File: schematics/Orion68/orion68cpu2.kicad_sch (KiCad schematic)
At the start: 46 parts, among them J1 clock, Q1 2N3904, Q2 2N3904, Q3 2N3904, SW2 reset, U0 74LS393, U1 MC68000P, U2 74LS541, U3 74LS541, U4 74LS541, U5 74LS245, U6 74LS245, U7 74LS541, U8 74LS148, Y1.2 16MHZ, Y2 16MHZ

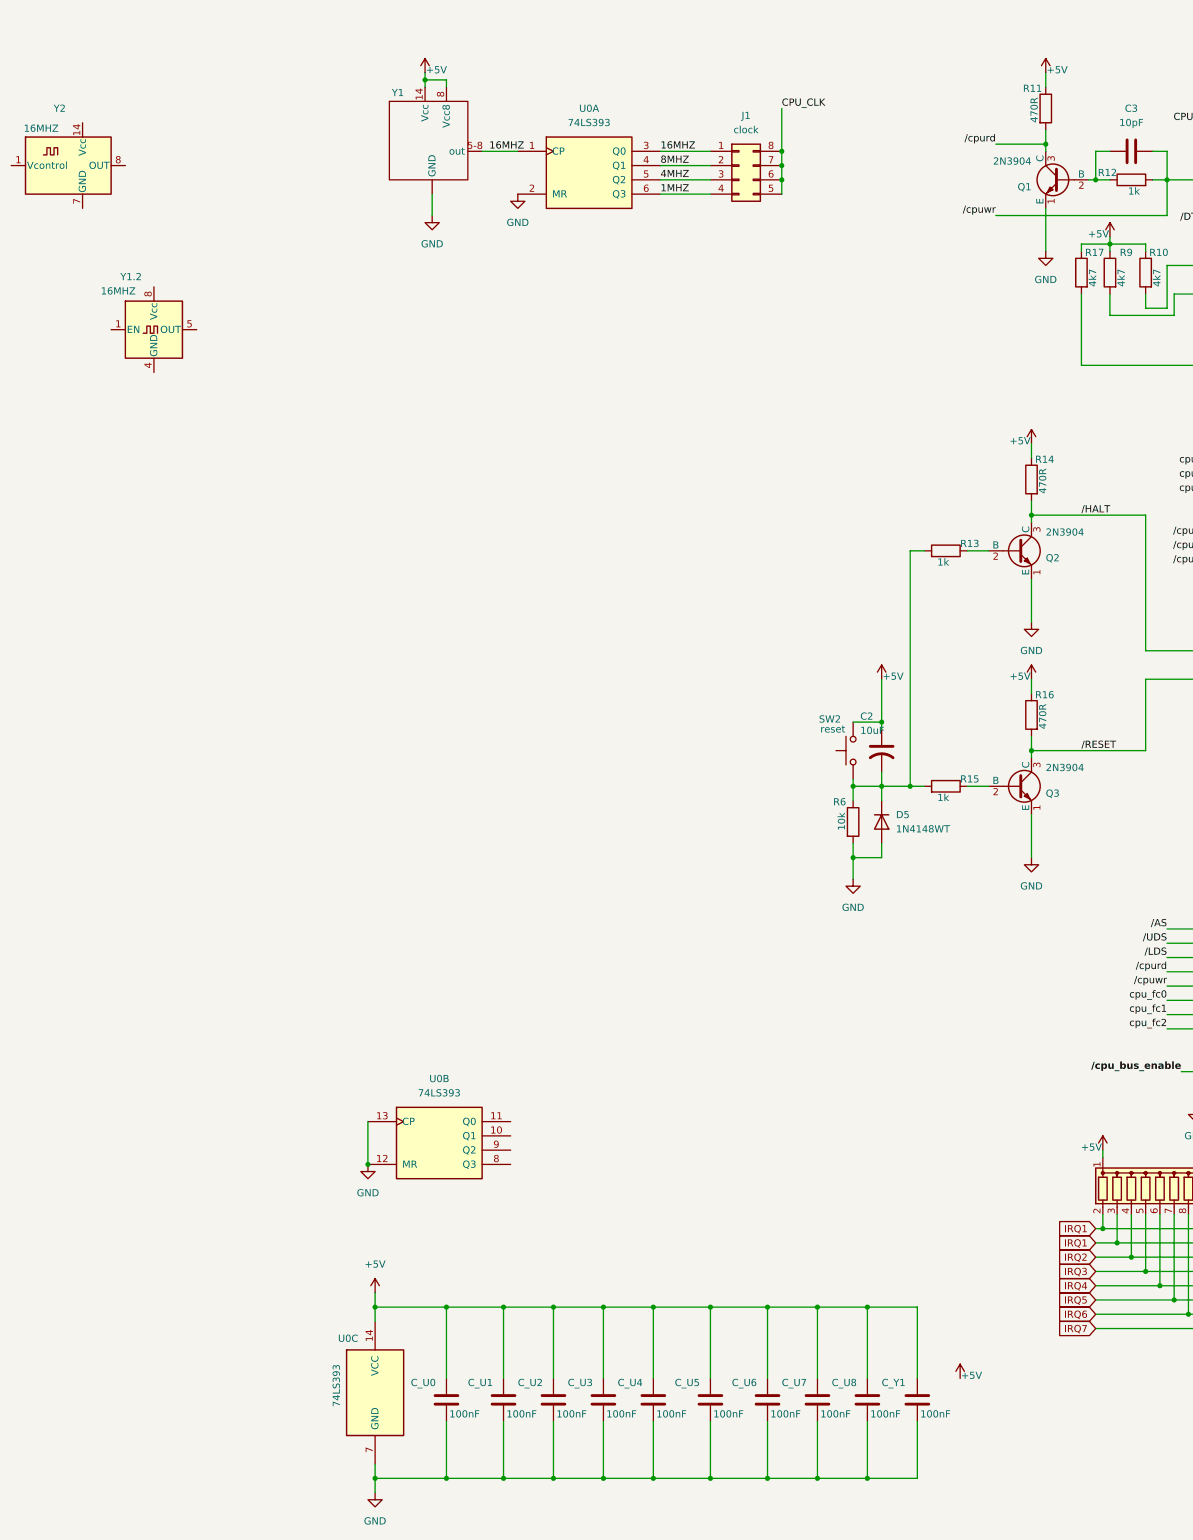
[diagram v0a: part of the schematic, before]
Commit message: Finished CPU board schematic
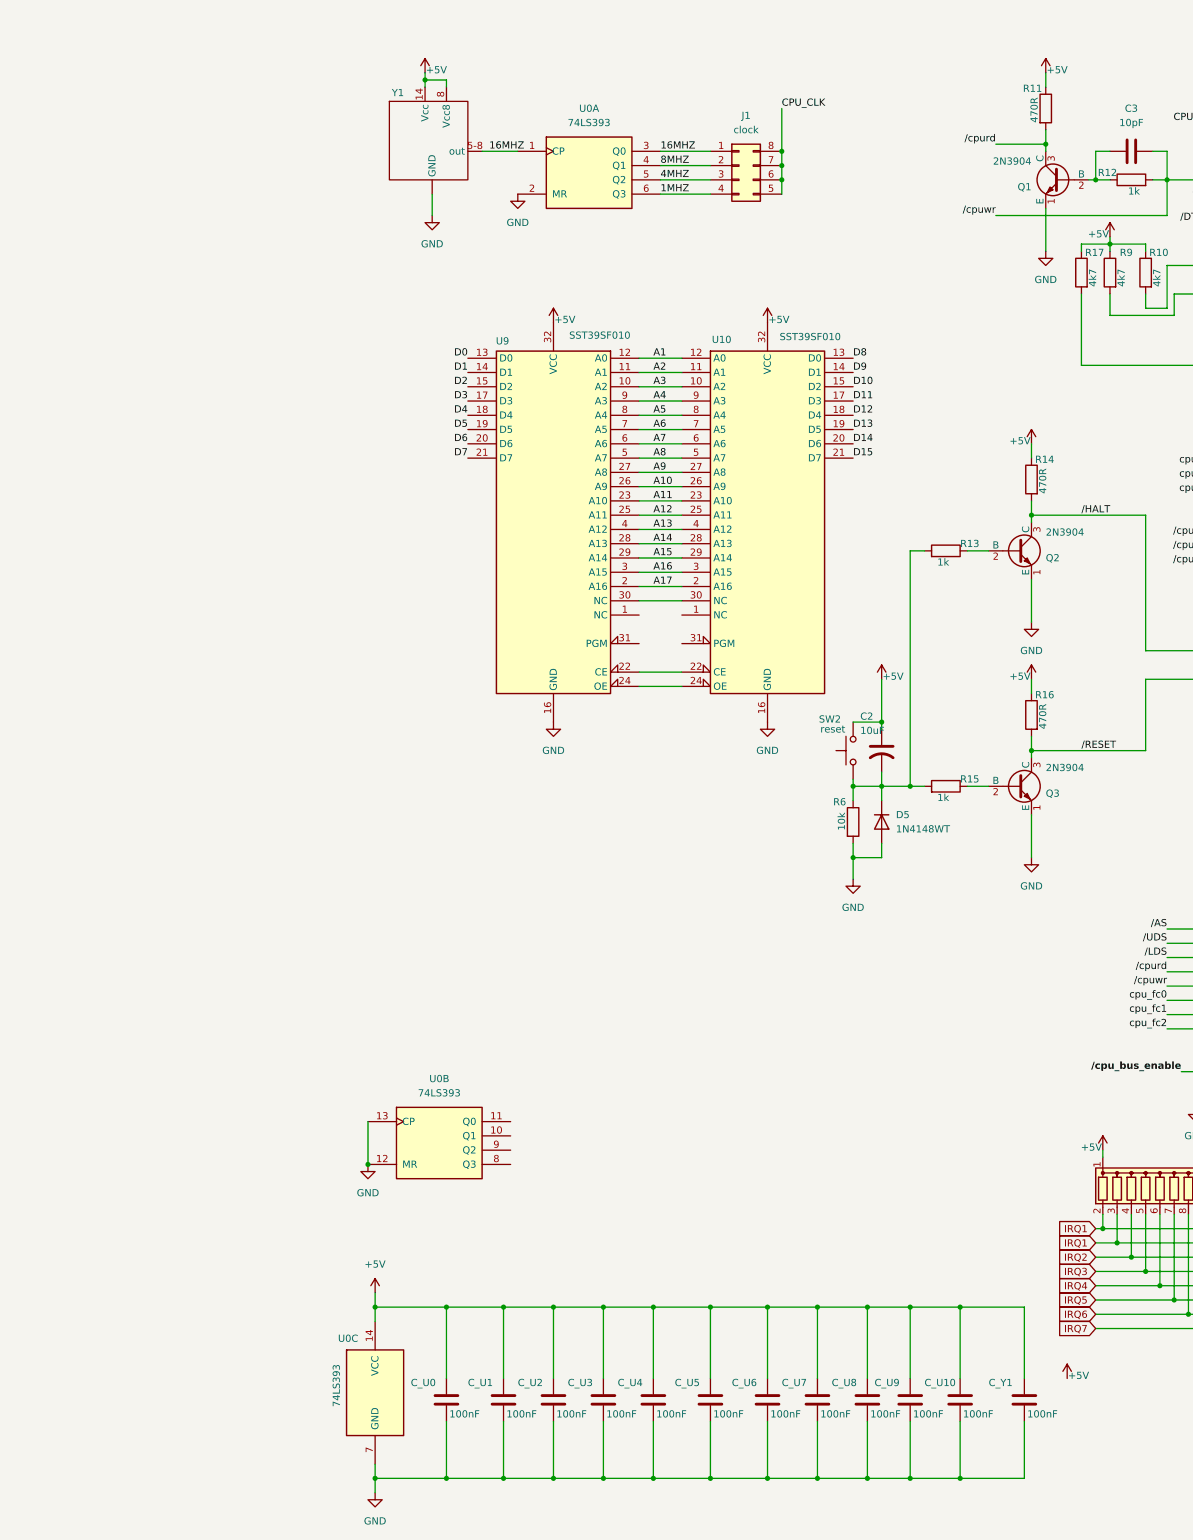
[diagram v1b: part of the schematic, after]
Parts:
- removed Y1.2: 16MHZ, Oscillator:Oscillator_DIP-8, symbol Oscillator:CXO_DIP8
- removed Y2: 16MHZ, Oscillator:Oscillator_DIP-14, symbol Oscillator:OCXO-14
- added C_U10, C_U9: 100nF, symbol Device:C
- added U10, U9: SST39SF010, symbol Memory_Flash:SST39SF010
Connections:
- net +5V: now also C_U10.1, C_U9.1, U10.32 (VCC), U9.32 (VCC)
- net A1: now also U10.12 (A0), U9.12 (A0)
- net A10: now also U10.26 (A9), U9.26 (A9)
- net A11: now also U10.23 (A10), U9.23 (A10)
- net A12: now also U10.25 (A11), U9.25 (A11)
- net A13: now also U10.4 (A12), U9.4 (A12)
- net A14: now also U10.28 (A13), U9.28 (A13)
- net A15: now also U10.29 (A14), U9.29 (A14)
- net A16: now also U10.3 (A15), U9.3 (A15)
- net A17: now also U10.2 (A16), U9.2 (A16)
- net A2: now also U10.11 (A1), U9.11 (A1)
- net A3: now also U10.10 (A2), U9.10 (A2)
- net A4: now also U10.9 (A3), U9.9 (A3)
- net A5: now also U10.8 (A4), U9.8 (A4)
- net A6: now also U10.7 (A5), U9.7 (A5)
- net A7: now also U10.6 (A6), U9.6 (A6)
- net A8: now also U10.5 (A7), U9.5 (A7)
- net A9: now also U10.27 (A8), U9.27 (A8)
- net D0: now also U9.13 (D0)
- net D1: now also U9.14 (D1)
- net D10: now also U10.15 (D2)
- net D11: now also U10.17 (D3)
- net D12: now also U10.18 (D4)
- net D13: now also U10.19 (D5)
- net D14: now also U10.20 (D6)
- net D15: now also U10.21 (D7)
- net D2: now also U9.15 (D2)
- net D3: now also U9.17 (D3)
- net D4: now also U9.18 (D4)
- net D5: now also U9.19 (D5)
- net D6: now also U9.20 (D6)
- net D7: now also U9.21 (D7)
- net D8: now also U10.13 (D0)
- net D9: now also U10.14 (D1)
- net GND: now also C_U10.2, C_U9.2, U10.16 (GND), U9.16 (GND)
- new net: U10.22 (CE), U9.22 (CE)
- new net: U10.24 (OE), U9.24 (OE)
- new net: U10.30 (NC), U9.30 (NC)
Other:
- moved on the sheet: C_Y1

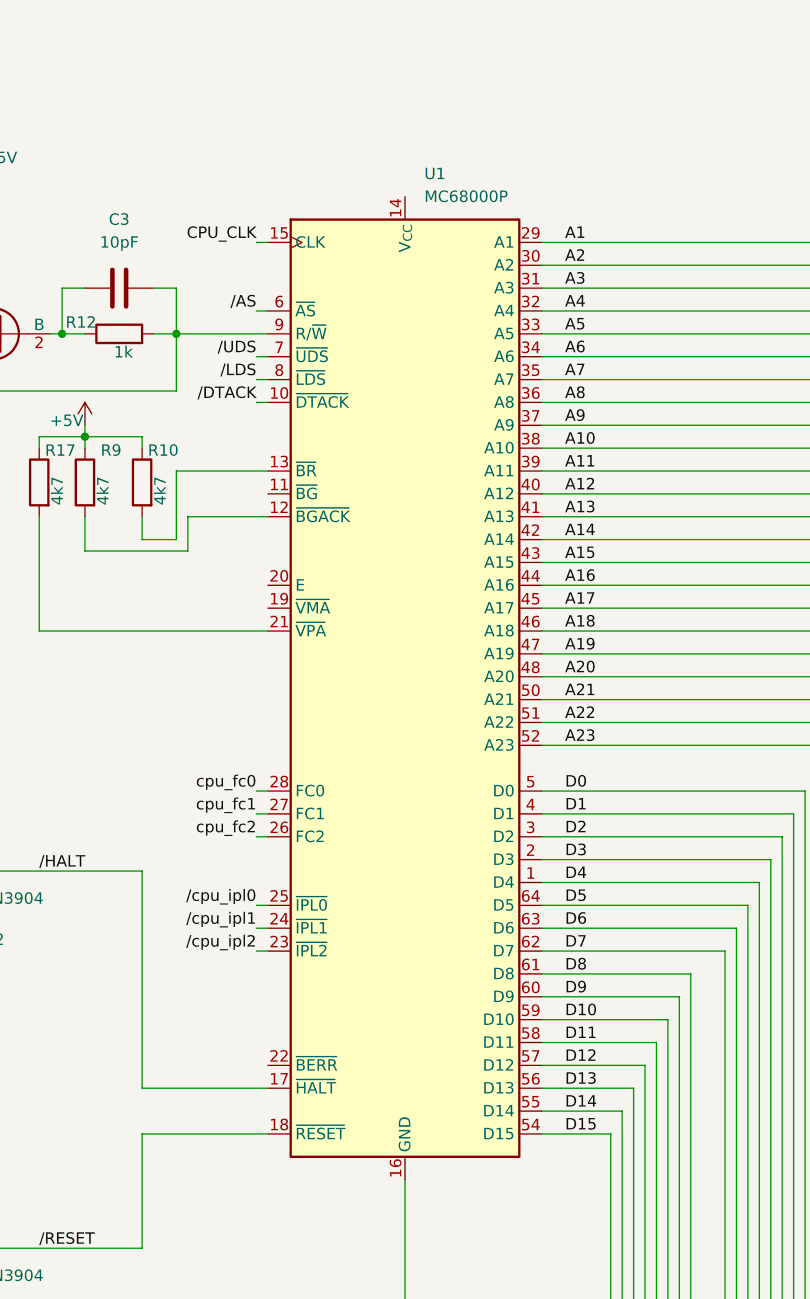
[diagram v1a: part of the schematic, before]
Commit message: changed 68k dip for plcc
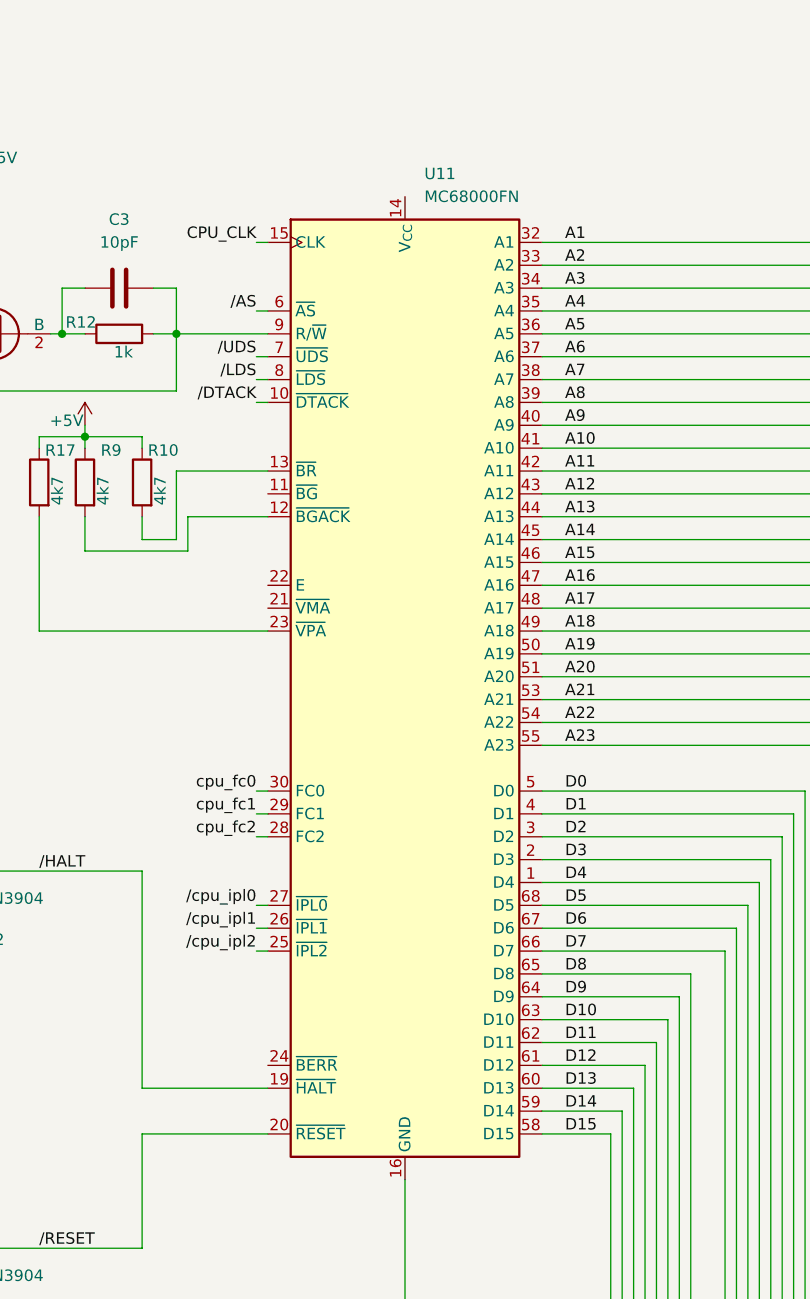
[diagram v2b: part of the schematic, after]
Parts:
- removed U1: MC68000P, Package_DIP:DIP-64_W22.86mm, symbol CPU_NXP_68000:MC68000P
- added U11: MC68000FN, Package_LCC:PLCC-68_24.2x24.2mm_P1.27mm, symbol CPU_NXP_68000:MC68000FN
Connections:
- net A1: now also U11.32 (A1)
- net A10: now also U11.41 (A10)
- net A11: now also U11.42 (A11)
- net A12: now also U11.43 (A12)
- net A13: now also U11.44 (A13)
- net A14: now also U11.45 (A14)
- net A15: now also U11.46 (A15)
- net A16: now also U11.47 (A16)
- net A17: now also U11.48 (A17)
- net A18: now also U11.49 (A18)
- net A19: now also U11.50 (A19)
- net A2: now also U11.33 (A2)
- net A20: now also U11.51 (A20)
- net A21: now also U11.53 (A21)
- net A22: now also U11.54 (A22)
- net A23: now also U11.55 (A23)
- net A3: now also U11.34 (A3)
- net A4: now also U11.35 (A4)
- net A5: now also U11.36 (A5)
- net A6: now also U11.37 (A6)
- net A7: now also U11.38 (A7)
- net A8: now also U11.39 (A8)
- net A9: now also U11.40 (A9)
- net CPU_CLK: now also U11.15 (CLK)
- net D0: now also U11.5 (D0)
- net D1: now also U11.4 (D1)
- net D10: now also U11.63 (D10)
- net D11: now also U11.62 (D11)
- net D12: now also U11.61 (D12)
- net D13: now also U11.60 (D13)
- net D14: now also U11.59 (D14)
- net D15: now also U11.58 (D15)
- net D2: now also U11.3 (D2)
- net D3: now also U11.2 (D3)
- net D4: now also U11.1 (D4)
- net D5: now also U11.68 (D5)
- net D6: now also U11.67 (D6)
- net D7: now also U11.66 (D7)
- net D8: now also U11.65 (D8)
- net D9: now also U11.64 (D9)
- net GND: now also U11.16 (GND), U11.17 (GND), U11.56 (GND), U11.57 (GND)
- net cpu_fc0: now also U11.30 (FC0)
- net cpu_fc1: now also U11.29 (FC1)
- net cpu_fc2: now also U11.28 (FC2)
- net /AS: now also U11.6 (~{AS})
- net /DTACK: now also U11.10 (~{DTACK})
- net /HALT: now also U11.19 (~{HALT})
- net /LDS: now also U11.8 (~{LDS})
- net /RESET: now also U11.20 (~{RESET})
- net /UDS: now also U11.7 (~{UDS})
- net /cpu_ipl0: now also U11.27 (~{IPL0})
- net /cpu_ipl1: now also U11.26 (~{IPL1})
- net /cpu_ipl2: now also U11.25 (~{IPL2})
- net /cpuwr: now also U11.9 (R/~{W})
- net at R9.2: now also U11.12 (~{BGACK})
- net at R10.2: now also U11.13 (~{BR})
- net at R17.2: now also U11.23 (~{VPA})
- new net: U11.14 (V_{CC}), U11.52 (V_{CC})

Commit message: updating
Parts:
- removed R7, R8: 470R, symbol Device:R
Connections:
- net +5V: now also U10.31 (PGM), U9.31 (PGM)
- net GND: now also D3.1 (K), D4.1 (K)
- net /halt: now also D3.2 (A)
- net /reset: now also D4.2 (A)
- net at U9.30 (NC): no longer U10.30 (NC)
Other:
- moved on the sheet: D3, D4

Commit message: Keyboard tested,code durty
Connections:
- net /BERR: now also U11.24 (~{BERR})
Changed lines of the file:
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@@
 	(wire
 		(pts
+			(xy 170.18 124.46) (xy 171.45 124.46)
+		)
+		(stroke
+			(width 0)
+			(type default)
+		)
+	)
+	(wire
+		(pts
 			(xy 157.48 132.08) (xy 157.48 144.78)
 		)
@@
 		)
 	)
+	(label "{slash}BERR"
+		(at 170.18 124.46 180)
+		(effects
+			(font
+				(size 1.27 1.27)
+			)
+			(justify right bottom)
+		)
+	)

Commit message: Updating cpu
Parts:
- added C_U14: 100nF, symbol Device:C
- added U12: GAL16V8, symbol Logic_Programmable:GAL16V8
- added U14: 74HC74, symbol 74xx:74HC74
- renumbered U11 to U0
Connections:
- net /reset is gone; now on net /RESET: D4.2 (A), J1.66
- net +5V: now also C_U14.1, U14.1 (~{R}), U14.14 (VCC)
- net 4MHZ: now also U12.1 (I1/CLK)
- net A20: now also U12.2 (I2)
- net A21: now also U12.3 (I3)
- net A22: now also U12.4 (I4)
- net A23: now also U12.5 (I5)
- net GND: now also C_U14.2, U12.10 (GND), U14.2 (D), U14.7 (GND)
- net /AS: now also U12.6 (I6)
- net /DTACK: now also U12.13 (IO7)
- net /LDS: now also U10.24 (OE)
- net /RESET: now also U12.8 (I8), U14.4 (~{S})
- net /UDS: now also U9.24 (OE)
- net /ROM_CS: now reaches U10.22 (CE), U9.22 (CE)
- net /ROM_CS: now also U12.19 (IO1)
- net reset renamed RESET
- net RESET: now also U12.14 (IO6)
- new net BOOT_SIG: U12.11 (I10/~{OE}), U14.5 (Q)
- new net R/W: U12.7 (I7)
- new net /IO_BOOT_KILL: U12.16 (IO4), U14.3 (C)
- new net /IO_CS: U12.17 (I03)
- new net /RAM_CS: U12.18 (IO2)
- new net /RD: U12.15 (IO5)
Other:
- moved on the sheet: C_U0, C_U1, C_U10, C_U2, C_U3, C_U4, C_U5, C_U6, C_U7, C_U8, C_U9, C_Y1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

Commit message: Updating cpu
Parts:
- added C_U0_2, C_U12: 100nF, Capacitor_THT:C_Disc_D4.3mm_W1.9mm_P5.00mm, symbol Device:C
- added D4: Led_Boot, Diode_THT:D_T-1_P5.08mm_Horizontal, symbol Device:LED
- C2: footprint (none) -> Capacitor_THT:CP_Radial_D5.0mm_P2.50mm
- C3, C_U1, C_U10, C_U2, C_U3, C_U4, C_U5, C_U6, C_U7, C_U8, C_U9, C_Y1: footprint (none) -> Capacitor_THT:C_Disc_D4.3mm_W1.9mm_P5.00mm
- C_U0_1: renamed from C_U0; footprint (none) -> Capacitor_THT:C_Disc_D4.3mm_W1.9mm_P5.00mm
- C_U11: renamed from C_U14; footprint (none) -> Capacitor_THT:C_Disc_D4.3mm_W1.9mm_P5.00mm
- D1: renamed from D5; footprint Diode_SMD:D_SOD-523 -> Diode_THT:D_T-1_P5.08mm_Horizontal
- D2: renamed from D3; value Halt -> Led_Halt; footprint (none) -> Diode_THT:D_T-1_P5.08mm_Horizontal
- D3: renamed from D4; value Reset -> Led_Reset; footprint (none) -> Diode_THT:D_T-1_P5.08mm_Horizontal
- J1: value ~ -> Euro96pin
- J2: renamed from J1; footprint (none) -> Connector_PinHeader_2.54mm:PinHeader_2x04_P2.54mm_Vertical
- R10: renamed from R16; footprint (none) -> Resistor_THT:R_Axial_DIN0204_L3.6mm_D1.6mm_P5.08mm_Horizontal
- R11, R6: footprint (none) -> Resistor_THT:R_Axial_DIN0204_L3.6mm_D1.6mm_P5.08mm_Horizontal
- R12: renamed from R17; footprint (none) -> Resistor_THT:R_Axial_DIN0204_L3.6mm_D1.6mm_P5.08mm_Horizontal
- R13: renamed from R9; footprint (none) -> Resistor_THT:R_Axial_DIN0204_L3.6mm_D1.6mm_P5.08mm_Horizontal
- R14: renamed from R12; footprint (none) -> Resistor_THT:R_Axial_DIN0204_L3.6mm_D1.6mm_P5.08mm_Horizontal
- R15: renamed from R10; footprint (none) -> Resistor_THT:R_Axial_DIN0204_L3.6mm_D1.6mm_P5.08mm_Horizontal
- R7: renamed from R13; footprint (none) -> Resistor_THT:R_Axial_DIN0204_L3.6mm_D1.6mm_P5.08mm_Horizontal
- R8: renamed from R15; footprint (none) -> Resistor_THT:R_Axial_DIN0204_L3.6mm_D1.6mm_P5.08mm_Horizontal
- R9: renamed from R14; footprint (none) -> Resistor_THT:R_Axial_DIN0204_L3.6mm_D1.6mm_P5.08mm_Horizontal
- SW2: value reset -> sw_reset; footprint (none) -> Button_Switch_THT:SW_Lever_1P2T_NKK_GW12LxH
- U1: renamed from U5; footprint (none) -> Package_DIP:DIP-20_W7.62mm
- U10, U9: footprint (none) -> Package_LCC:PLCC-32_THT-Socket
- U11: renamed from U14; footprint (none) -> Package_DIP:DIP-14_W7.62mm
- U12: renamed from U0; footprint (none) -> Package_DIP:DIP-14_W7.62mm
- U2: renamed from U6; footprint (none) -> Package_DIP:DIP-20_W7.62mm
- U3: renamed from U2; footprint (none) -> Package_DIP:DIP-20_W7.62mm
- U4: renamed from U3; footprint (none) -> Package_DIP:DIP-20_W7.62mm
- U5: renamed from U4; footprint (none) -> Package_DIP:DIP-20_W7.62mm
- U6: renamed from U7; footprint (none) -> Package_DIP:DIP-20_W7.62mm
- U7: renamed from U8; footprint (none) -> Package_DIP:DIP-16_W7.62mm
- U8: renamed from U12; footprint (none) -> Package_DIP:DIP-20_W7.62mm
- Y2: renamed from Y1; footprint (none) -> Package_DIP:DIP-14_W7.62mm
- renumbered Q2 to Q1, Q3 to Q2, Q1 to Q3
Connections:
- net +5V: now also C_U0_2.1, C_U12.1
- net BOOT_SIG: now also D4.2 (A)
- net GND: now also C_U0_2.2, C_U12.2, D4.1 (K)
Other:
- moved on the sheet: C_U1, C_U10, C_U11, C_U2, C_U3, C_U4, C_U5, C_U6, C_U7, C_U8, C_U9, C_Y1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

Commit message: First cpu test
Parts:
- added R1: 4k7, Resistor_THT:R_Axial_DIN0204_L3.6mm_D1.6mm_P5.08mm_Horizontal, symbol Device:R
- added R2: 220R, Resistor_THT:R_Axial_DIN0204_L3.6mm_D1.6mm_P5.08mm_Horizontal, symbol Device:R
- U0: footprint Package_LCC:PLCC-68_24.2x24.2mm_P1.27mm -> Package_LCC:PLCC-68_THT-Socket
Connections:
- net /cpuwr is gone; now on net R/W: C3.2, R14.2, U0.9 (R/~{W}), U6.6 (A4)
- net /halt is gone; now on net /HALT: D2.2 (A)
- net +5V: now also U0.14 (V_{CC}), U0.52 (V_{CC}), U8.20 (VCC), Y2.11 (Vcc8), R1.1; no longer Y2.8 (Vcc8)
- net 16MHZ: now also Y2.8; no longer J2.1 (Pin_1), U12.3 (Q0), Y2.5-8 (out)
- net 1MHZ: now also J2.8 (Pin_8); no longer J2.4 (Pin_4)
- net 4MHZ: now also J2.4 (Pin_4), U12.4 (Q1); no longer J2.3 (Pin_3), U12.5 (Q2)
- net 8MHZ: now also U12.3 (Q0); no longer U12.4 (Q1)
- net CPU_CLK: now also J2.1 (Pin_1), J2.3 (Pin_3); no longer J2.6 (Pin_6), J2.8 (Pin_8)
- net GND: now also U7.10 (IO), Y2.7 (GND); no longer Y2. (GND)
- net IRQ1: no longer RN1.2 (R1), U7.10 (IO)
- net R/W: no longer U8.7 (I7)
- net /BERR: now also R1.2
- net /LDS: now also U9.24 (OE); no longer U10.24 (OE)
- net /UDS: now also U10.24 (OE); no longer U9.24 (OE)
- net at C2.2, D1.1 (K), R6.1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: now also R2.2
- net BOOTIN: now reaches U8.9 (I9)
- net BOOTIN: now also D4.2 (A), U11.5 (Q)
- net PWR_GOOD_IN: now reaches J1.88
- removed net BOOT_SIG: D4.2 (A), U11.5 (Q), U8.11 (I10/~{OE})
- net /IO_BOOT_KILL renamed /KILLBT
- net /RD: no longer names the net of U8.15 (IO5)
- new net 2MHZ: J2.6 (Pin_6), U12.5 (Q2)
- new net PWR_GOOD: R2.1
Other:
- note added: "Azul"
- note added: "Verde"
- note added: "Vermelho"
- moved on the sheet: D2, D3, D4, J2, RN1, U11A, U11B, U12A, U12B, U7, U8, U9
